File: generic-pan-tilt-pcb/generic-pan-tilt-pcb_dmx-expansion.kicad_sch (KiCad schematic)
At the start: 3 parts, among them J11 Conn_01x08, J12 Conn_01x08, J13 Conn_01x05

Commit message: rename again to generic-pan-tilt
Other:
- title: Pan Tilt PCB: DMX Port Expansion -> Generic Pan Tilt PCB: DMX Port Expansion
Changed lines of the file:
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@@
 	(paper "USLetter")
 	(title_block
-		(title "Pan Tilt PCB: DMX Port Expansion")
+		(title "Generic Pan Tilt PCB: DMX Port Expansion")
 		(date "2024-07-10")
 		(company "Responsive Environments, MIT Media Lab")
@@
 		)
 		(instances
-			(project "pan-tilt-pcb"
+			(project "generic-pan-tilt-pcb"
 				(path "/e3bbbe58-bf8f-42a8-8505-028de8235dc1/e2b5314f-806a-4f39-8c59-debbd2a2bba5"
 					(reference "#PWR060")
@@
 		)
 		(instances
-			(project "pan-tilt-pcb"
+			(project "generic-pan-tilt-pcb"
 				(path "/e3bbbe58-bf8f-42a8-8505-028de8235dc1/e2b5314f-806a-4f39-8c59-debbd2a2bba5"
 					(reference "J13")
@@
 		)
 		(instances
-			(project "pan-tilt-pcb"
+			(project "generic-pan-tilt-pcb"
 				(path "/e3bbbe58-bf8f-42a8-8505-028de8235dc1/e2b5314f-806a-4f39-8c59-debbd2a2bba5"
 					(reference "#PWR061")
@@
 		)
 		(instances
-			(project "pan-tilt-pcb"
+			(project "generic-pan-tilt-pcb"
 				(path "/e3bbbe58-bf8f-42a8-8505-028de8235dc1/e2b5314f-806a-4f39-8c59-debbd2a2bba5"
 					(reference "J12")
@@
 		)
 		(instances
-			(project "pan-tilt-pcb"
+			(project "generic-pan-tilt-pcb"
 				(path "/e3bbbe58-bf8f-42a8-8505-028de8235dc1/e2b5314f-806a-4f39-8c59-debbd2a2bba5"
 					(reference "#PWR063")
@@
 		)
 		(instances
-			(project "pan-tilt-pcb"
+			(project "generic-pan-tilt-pcb"
 				(path "/e3bbbe58-bf8f-42a8-8505-028de8235dc1/e2b5314f-806a-4f39-8c59-debbd2a2bba5"
 					(reference "#PWR062")
@@
 		)
 		(instances
-			(project "pan-tilt-pcb"
+			(project "generic-pan-tilt-pcb"
 				(path "/e3bbbe58-bf8f-42a8-8505-028de8235dc1/e2b5314f-806a-4f39-8c59-debbd2a2bba5"
 					(reference "J11")

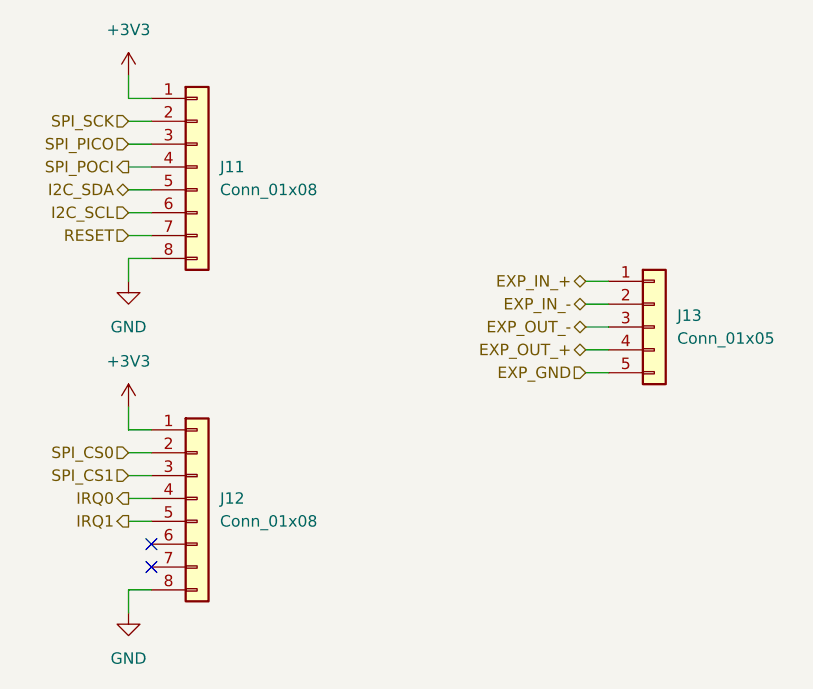
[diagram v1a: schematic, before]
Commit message: pick all footprints, begin layout
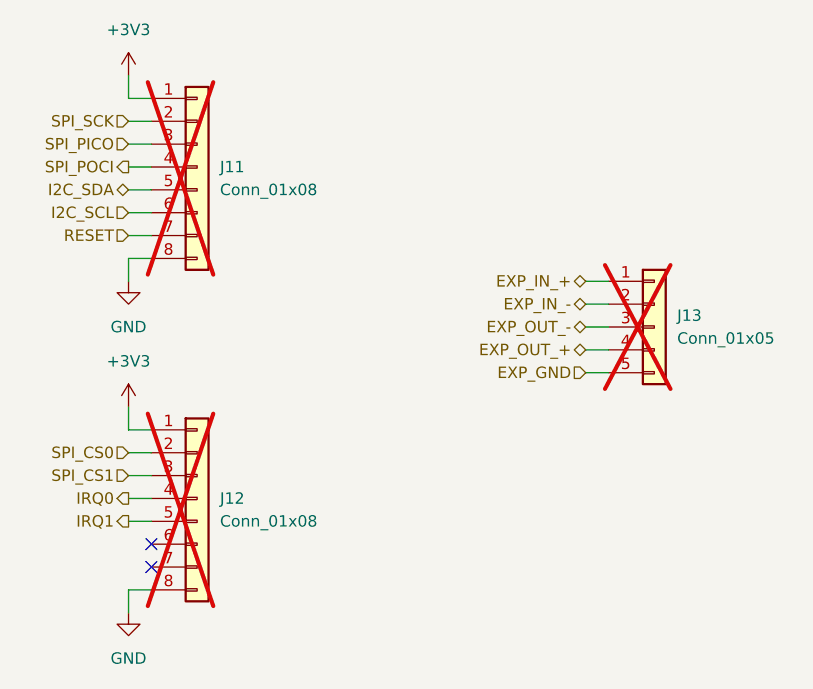
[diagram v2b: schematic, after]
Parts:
- J11, J12: footprint (none) -> Connector_PinHeader_2.54mm:PinHeader_1x08_P2.54mm_Vertical; now not fitted
- J13: footprint (none) -> Connector_PinHeader_2.54mm:PinHeader_1x05_P2.54mm_Vertical; now not fitted
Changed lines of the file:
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@@
 		(dnp no)
 		(fields_autoplaced yes)
-		(property "Reference" "#PWR060"
+		(property "Reference" "#PWR059"
 			(at 121.92 68.58 0)
 			(effects
@@
 			(project "generic-pan-tilt-pcb"
 				(path "/e3bbbe58-bf8f-42a8-8505-028de8235dc1/e2b5314f-806a-4f39-8c59-debbd2a2bba5"
-					(reference "#PWR060")
+					(reference "#PWR059")
 					(unit 1)
 				)
@@
 		(in_bom yes)
 		(on_board yes)
-		(dnp no)
+		(dnp yes)
 		(fields_autoplaced yes)
 		(property "Reference" "J13"
@@
 			)
 		)
-		(property "Footprint" ""
+		(property "Footprint" "Connector_PinHeader_2.54mm:PinHeader_1x05_P2.54mm_Vertical"
 			(at 180.34 92.71 0)
 			(effects
@@
 		(dnp no)
 		(fields_autoplaced yes)
-		(property "Reference" "#PWR061"
+		(property "Reference" "#PWR060"
 			(at 121.92 93.98 0)
 			(effects
@@
 			(project "generic-pan-tilt-pcb"
 				(path "/e3bbbe58-bf8f-42a8-8505-028de8235dc1/e2b5314f-806a-4f39-8c59-debbd2a2bba5"
-					(reference "#PWR061")
+					(reference "#PWR060")
 					(unit 1)
 				)
@@
 		(in_bom yes)
 		(on_board yes)
-		(dnp no)
+		(dnp yes)
 		(fields_autoplaced yes)
 		(property "Reference" "J12"
@@
 			)
 		)
-		(property "Footprint" ""
+		(property "Footprint" "Connector_PinHeader_2.54mm:PinHeader_1x08_P2.54mm_Vertical"
 			(at 129.54 111.76 0)
 			(effects
@@
 		(dnp no)
 		(fields_autoplaced yes)
-		(property "Reference" "#PWR063"
+		(property "Reference" "#PWR062"
 			(at 121.92 130.81 0)
 			(effects
@@
 			(project "generic-pan-tilt-pcb"
 				(path "/e3bbbe58-bf8f-42a8-8505-028de8235dc1/e2b5314f-806a-4f39-8c59-debbd2a2bba5"
-					(reference "#PWR063")
+					(reference "#PWR062")
 					(unit 1)
 				)
@@
 		(dnp no)
 		(fields_autoplaced yes)
-		(property "Reference" "#PWR062"
+		(property "Reference" "#PWR061"
 			(at 121.92 105.41 0)
 			(effects
@@
 			(project "generic-pan-tilt-pcb"
 				(path "/e3bbbe58-bf8f-42a8-8505-028de8235dc1/e2b5314f-806a-4f39-8c59-debbd2a2bba5"
-					(reference "#PWR062")
+					(reference "#PWR061")
 					(unit 1)
 				)
@@
 		(in_bom yes)
 		(on_board yes)
-		(dnp no)
+		(dnp yes)
 		(fields_autoplaced yes)
 		(property "Reference" "J11"
@@
 			)
 		)
-		(property "Footprint" ""
+		(property "Footprint" "Connector_PinHeader_2.54mm:PinHeader_1x08_P2.54mm_Vertical"
 			(at 129.54 74.93 0)
 			(effects

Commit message: begin new routing
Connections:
- net +3V3: now also J11.8 (Pin_8), J12.8 (Pin_8); no longer J11.1 (Pin_1), J12.1 (Pin_1)
- net EXP_GND: now also J13.1 (Pin_1); no longer J13.5 (Pin_5)
- net EXP_IN_+: now also J13.5 (Pin_5); no longer J13.1 (Pin_1)
- net EXP_IN_-: now also J13.4 (Pin_4); no longer J13.2 (Pin_2)
- net EXP_OUT_+: now also J13.2 (Pin_2); no longer J13.4 (Pin_4)
- net GND: now also J11.1 (Pin_1), J12.1 (Pin_1); no longer J11.8 (Pin_8), J12.8 (Pin_8)
- net I2C_SCL: now also J11.3 (Pin_3); no longer J11.6 (Pin_6)
- net I2C_SDA: now also J11.4 (Pin_4); no longer J11.5 (Pin_5)
- net IRQ0: now also J12.5 (Pin_5); no longer J12.4 (Pin_4)
- net IRQ1: now also J12.4 (Pin_4); no longer J12.5 (Pin_5)
- net RESET: now also J11.2 (Pin_2); no longer J11.7 (Pin_7)
- net SPI_CS0: now also J12.7 (Pin_7); no longer J12.2 (Pin_2)
- net SPI_CS1: now also J12.6 (Pin_6); no longer J12.3 (Pin_3)
- net SPI_PICO: now also J11.6 (Pin_6); no longer J11.3 (Pin_3)
- net SPI_POCI: now also J11.5 (Pin_5); no longer J11.4 (Pin_4)
- net SPI_SCK: now also J11.7 (Pin_7); no longer J11.2 (Pin_2)
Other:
- moved on the sheet: J11, J12, J13

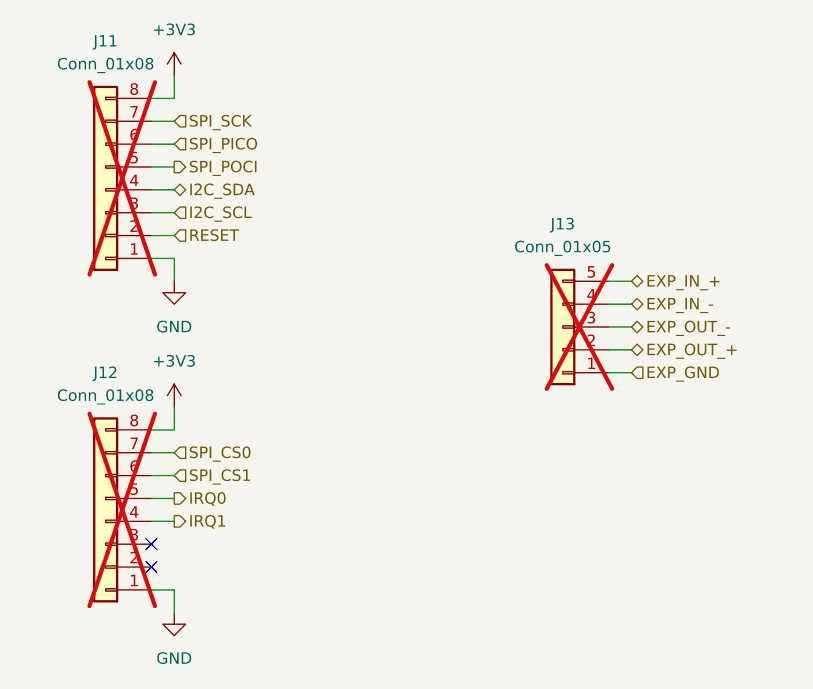
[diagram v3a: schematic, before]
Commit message: finish rp2040 layout
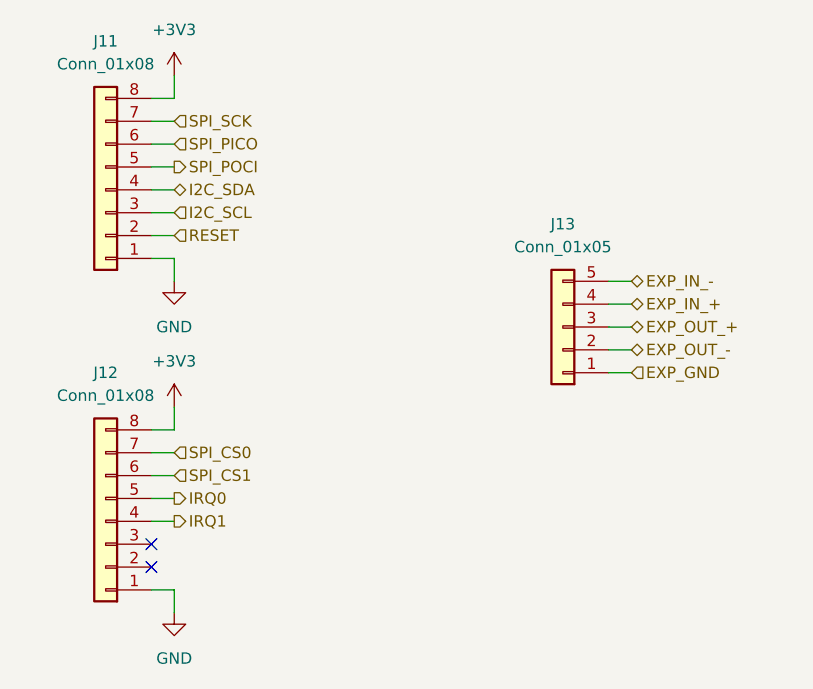
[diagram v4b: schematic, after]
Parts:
- J11, J12: footprint Connector_PinHeader_2.54mm:PinHeader_1x08_P2.54mm_Vertical -> Connector_PinSocket_2.54mm:PinSocket_1x08_P2.54mm_Vertical; now fitted
- J13: footprint Connector_PinHeader_2.54mm:PinHeader_1x05_P2.54mm_Vertical -> Connector_PinSocket_2.54mm:PinSocket_1x05_P2.54mm_Vertical; now fitted
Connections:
- net EXP_IN_+: now also J13.4 (Pin_4); no longer J13.5 (Pin_5)
- net EXP_IN_-: now also J13.5 (Pin_5); no longer J13.4 (Pin_4)
- net EXP_OUT_+: now also J13.3 (Pin_3); no longer J13.2 (Pin_2)
- net EXP_OUT_-: now also J13.2 (Pin_2); no longer J13.3 (Pin_3)
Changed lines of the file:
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@@
 	(hierarchical_label "EXP_OUT_+"
 		(shape bidirectional)
-		(at 177.8 95.25 0)
+		(at 177.8 92.71 0)
 		(fields_autoplaced yes)
 		(effects
@@
 	(hierarchical_label "EXP_IN_+"
 		(shape bidirectional)
-		(at 177.8 87.63 0)
+		(at 177.8 90.17 0)
 		(fields_autoplaced yes)
 		(effects
@@
 	(hierarchical_label "EXP_OUT_-"
 		(shape bidirectional)
-		(at 177.8 92.71 0)
+		(at 177.8 95.25 0)
 		(fields_autoplaced yes)
 		(effects
@@
 	(hierarchical_label "EXP_IN_-"
 		(shape bidirectional)
-		(at 177.8 90.17 0)
+		(at 177.8 87.63 0)
 		(fields_autoplaced yes)
 		(effects
@@
 		(in_bom yes)
 		(on_board yes)
-		(dnp yes)
+		(dnp no)
 		(fields_autoplaced yes)
 		(property "Reference" "J13"
@@
 			)
 		)
-		(property "Footprint" "Connector_PinHeader_2.54mm:PinHeader_1x05_P2.54mm_Vertical"
+		(property "Footprint" "Connector_PinSocket_2.54mm:PinSocket_1x05_P2.54mm_Vertical"
 			(at 170.18 92.71 0)
 			(effects
@@
 		(in_bom yes)
 		(on_board yes)
-		(dnp yes)
+		(dnp no)
 		(fields_autoplaced yes)
 		(property "Reference" "J12"
@@
 			)
 		)
-		(property "Footprint" "Connector_PinHeader_2.54mm:PinHeader_1x08_P2.54mm_Vertical"
+		(property "Footprint" "Connector_PinSocket_2.54mm:PinSocket_1x08_P2.54mm_Vertical"
 			(at 119.38 114.3 0)
 			(effects
@@
 		(in_bom yes)
 		(on_board yes)
-		(dnp yes)
+		(dnp no)
 		(property "Reference" "J11"
 			(at 119.38 60.96 0)
@@
 			)
 		)
-		(property "Footprint" "Connector_PinHeader_2.54mm:PinHeader_1x08_P2.54mm_Vertical"
+		(property "Footprint" "Connector_PinSocket_2.54mm:PinSocket_1x08_P2.54mm_Vertical"
 			(at 119.38 77.47 0)
 			(effects

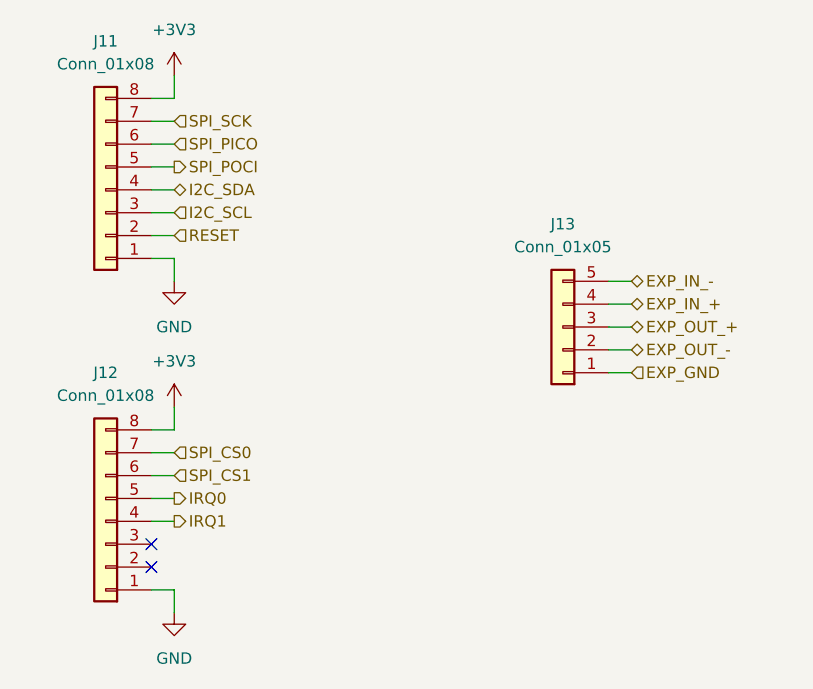
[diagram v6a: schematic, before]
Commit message: main dnp headers
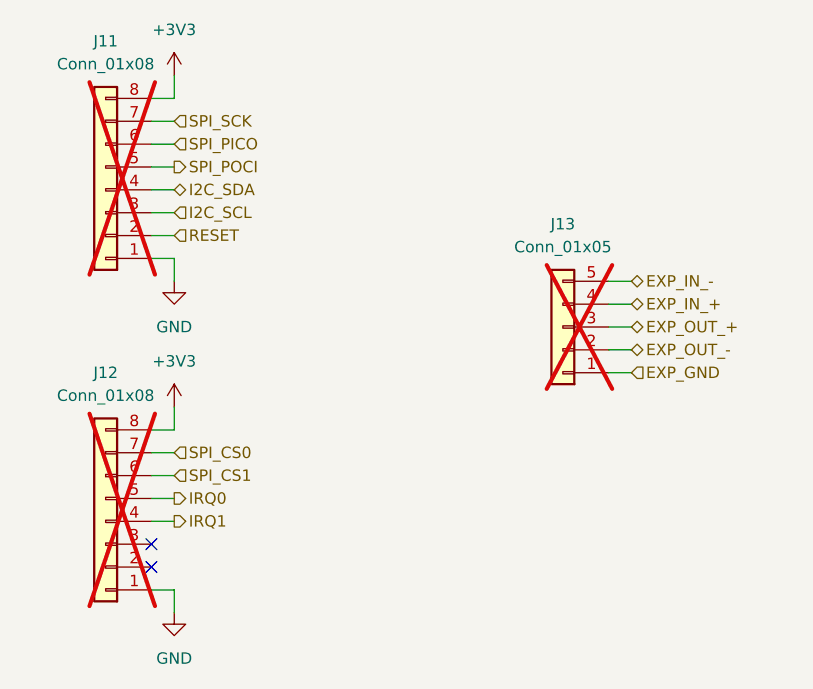
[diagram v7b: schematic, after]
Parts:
- J11, J12, J13: now not fitted; now left out of the parts list
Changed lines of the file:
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@@
 		(unit 1)
 		(exclude_from_sim no)
-		(in_bom yes)
-		(on_board yes)
-		(dnp no)
+		(in_bom no)
+		(on_board yes)
+		(dnp yes)
 		(fields_autoplaced yes)
 		(property "Reference" "J13"
@@
 		(unit 1)
 		(exclude_from_sim no)
-		(in_bom yes)
-		(on_board yes)
-		(dnp no)
+		(in_bom no)
+		(on_board yes)
+		(dnp yes)
 		(fields_autoplaced yes)
 		(property "Reference" "J12"
@@
 		(unit 1)
 		(exclude_from_sim no)
-		(in_bom yes)
-		(on_board yes)
-		(dnp no)
+		(in_bom no)
+		(on_board yes)
+		(dnp yes)
 		(property "Reference" "J11"
 			(at 119.38 60.96 0)
